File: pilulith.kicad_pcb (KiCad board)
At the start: 6 copper layers, 22 x 22 mm, 84 parts, among them J101 Conn_01x03_Pin, Q1 SBC847, SW101 CK_KMS2xxG, SW102 CK_KMS2xxG, U10 LIS2DH, U101 NRF52840-CKAA-F-R, U102 WLA.04, U103 ATECC608B-MAHDA, U104 LF21115TMR, U105 BME280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

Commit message: DRC passes
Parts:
- moved R112 0.51 mm to (157.5, 93.7)
- moved U10 0.08 mm to (159.4, 104.1)
- moved LS1 0.06 mm to (158.3, 111.1)
- moved C120 0.05 mm to (154.0, 96.5)
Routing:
- net GND: track 15.2 -> 16.8 mm, vias 94 -> 95
- net VCC: track 14.1 -> 15.4 mm, vias 29 -> 28
- net Net-(D112-K): track 0.84 -> 1.34 mm
- net /NFC2: vias 13 -> 5

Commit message: Removing additional warnings
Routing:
- net /IMU_INT: track 13.2 -> 11.3 mm, vias 3 -> 2
- net /DEC4_6: track 10.3 -> 8.72 mm, vias 11 -> 2
- net /LED02: vias 7 -> 3
- net /LED06: vias 5 -> 4
- net /LED07: vias 4 -> 3
- net /1.00/T0: vias 5 -> 4
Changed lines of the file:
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@@
 	)
 	(segment
+		(start 163.573771 100.892)
+		(end 163.573771 100.823833)
+		(width 0.0889)
+		(layer "F.Cu")
+		(net 3)
+	)
+	(segment
 		(start 161.919433 99.777445)
 		(end 162.527383 99.777445)
@@
 	)
 	(segment
-		(start 163.573771 100.823833)
-		(end 163.573771 100.892)
-		(width 0.0889)
-		(layer "F.Cu")
-		(net 3)
-	)
-	(segment
 		(start 161.574466 98.703224)
 		(end 161.574466 99.432478)
@@
 	)
 	(via
-		(at 163.577315 100.877)
-		(size 0.25)
-		(drill 0.15)
-		(layers "F.Cu" "B.Cu")
-		(net 3)
-	)
-	(via
-		(at 163.577315 100.877)
-		(size 0.25)
-		(drill 0.15)
-		(layers "F.Cu" "B.Cu")
-		(net 3)
-	)
-	(via
-		(at 163.577315 100.877)
-		(size 0.25)
-		(drill 0.15)
-		(layers "F.Cu" "B.Cu")
-		(net 3)
-	)
-	(via
-		(at 165.067051 100.587306)
-		(size 0.25)
-		(drill 0.15)
-		(layers "F.Cu" "B.Cu")
-		(net 3)
-	)
-	(via
-		(at 163.577315 100.877)
-		(size 0.25)
-		(drill 0.15)
-		(layers "F.Cu" "B.Cu")
-		(net 3)
-	)
-	(via
-		(at 163.577315 100.877)
-		(size 0.25)
-		(drill 0.15)
-		(layers "F.Cu" "B.Cu")
-		(net 3)
-	)
-	(via
-		(at 163.577315 100.877)
+		(at 163.573771 100.823833)
 		(size 0.25)
 		(drill 0.15)
@@
 		(net 3)
 	)
-	(via
-		(at 163.577315 100.877)
-		(size 0.25)
-		(drill 0.15)
-		(layers "F.Cu" "B.Cu")
-		(net 3)
-	)
-	(via
-		(at 163.577315 100.877)
-		(size 0.25)
-		(drill 0.15)
-		(layers "F.Cu" "B.Cu")
-		(net 3)
-	)
-	(via
-		(at 163.577315 100.877)
-		(size 0.25)
-		(drill 0.15)
-		(layers "F.Cu" "B.Cu")
-		(net 3)
-	)
 	(segment
 		(start 163.569013 98.052851)
@@
 	)
 	(segment
-		(start 164.777357 100.877)
-		(end 165.067051 100.587306)
-		(width 0.0889)
-		(layer "In3.Cu")
-		(net 3)
-	)
-	(segment
-		(start 163.577315 100.877)
-		(end 164.777357 100.877)
-		(width 0.0889)
-		(layer "In3.Cu")
-		(net 3)
-	)
-	(segment
 		(start 161.163245 95.539218)
 		(end 161.423463 95.279)
@@
 	)
 	(segment
-		(start 153.160814 96.228499)
-		(end 153.111314 96.278)
-		(width 0.0889)
-		(layer "In4.Cu")
-		(net 4)
-	)
-	(segment
-		(start 153.160814 96.228499)
+		(start 154.800314 94.588999)
 		(end 152.965315 96.423998)
 		(width 0.0889)
@@
 	)
 	(segment
-		(start 152.965315 96.423998)
-		(end 152.965315 96.66)
-		(width 0.0889)
-		(layer "In4.Cu")
-		(net 4)
-	)
-	(segment
 		(start 154.869314 94.52)
 		(end 154.800314 94.588999)
@@
 	)
 	(segment
-		(start 154.800314 94.588999)
-		(end 153.160814 96.228499)
+		(start 152.965315 96.423998)
+		(end 152.965315 96.66)
 		(width 0.0889)
 		(layer "In4.Cu")
@@
 	)
 	(segment
-		(start 159.492315 106.278)
-		(end 160.362315 106.278)
+		(start 159.501315 106.025)
+		(end 159.754315 106.278)
 		(width 0.0889)
 		(layer "F.Cu")
@@
 	(segment
 		(start 159.501315 105.424)
-		(end 159.492315 106.278)
+		(end 159.501315 106.025)
 		(width 0.0889)
 		(layer "F.Cu")
@@
 	)
 	(segment
-		(start 160.362315 106.278)
-		(end 160.574315 106.49)
+		(start 159.685313 104.762499)
+		(end 159.693315 105.265)
 		(width 0.0889)
 		(layer "F.Cu")
@@
 	)
 	(segment
-		(start 159.685313 104.762499)
-		(end 159.693315 105.265)
+		(start 159.754315 106.278)
+		(end 160.362315 106.278)
 		(width 0.0889)
 		(layer "F.Cu")
@@
 		(net 34)
 	)
-	(via
-		(at 160.066357 98.185648)
-		(size 0.25)
-		(drill 0.15)
-		(layers "F.Cu" "B.Cu")
-		(locked yes)
+	(segment
+		(start 160.362315 106.278)
+		(end 160.574315 106.49)
+		(width 0.0889)
+		(layer "F.Cu")
 		(net 34)
 	)
 	(via
-		(at 159.492315 106.278)
+		(at 160.066357 98.185648)
 		(size 0.25)
 		(drill 0.15)
 		(layers "F.Cu" "B.Cu")
+		(locked yes)
 		(net 34)
 	)
@@
 	)
 	(segment
-		(start 159.258463 98.287)
-		(end 159.058463 98.087)
-		(width 0.0889)
-		(layer "In3.Cu")
-		(net 34)
-	)
-	(segment
-		(start 159.058463 98.087)
-		(end 158.497463 98.087)
-		(width 0.0889)
-		(layer "In3.Cu")
-		(net 34)
-	)
-	(segment
-		(start 159.966898 98.287)
-		(end 159.258463 98.287)
-		(width 0.0889)
-		(layer "In3.Cu")
-		(net 34)
-	)
-	(segment
-		(start 160.067573 98.186325)
-		(end 159.966898 98.287)
-		(width 0.0889)
-		(layer "In3.Cu")
-		(net 34)
-	)
-	(segment
 		(start 159.941557 98.310448)
 		(end 159.941557 100.961767)
@@
 	)
 	(via
-		(at 166.922315 99.636)
-		(size 0.25)
-		(drill 0.15)
-		(layers "F.Cu" "B.Cu")
-		(net 50)
-	)
-	(via
-		(at 166.922315 99.636)
-		(size 0.25)
-		(drill 0.15)
-		(layers "F.Cu" "B.Cu")
-		(net 50)
-	)
-	(via
-		(at 166.922315 99.636)
-		(size 0.25)
-		(drill 0.15)
-		(layers "F.Cu" "B.Cu")
-		(net 50)
-	)
-	(via
-		(at 166.922315 99.636)
-		(size 0.25)
-		(drill 0.15)
-		(layers "F.Cu" "B.Cu")
-		(net 50)
-	)
-	(via
 		(at 168.729315 99.045)
 		(size 0.25)
@@
 	)
 	(via
-		(at 166.922315 99.636)
+		(at 166.928315 99.638)
 		(size 0.25)
 		(drill 0.15)
@@
 	)
 	(segment
+		(start 166.926315 99.636)
+		(end 166.928315 99.638)
+		(width 0.0889)
+		(layer "In3.Cu")
+		(net 50)
+	)
+	(segment
 		(start 164.987031 100.19545)
 		(end 164.746173 100.436308)
@@
 	)
 	(segment
+		(start 166.922315 99.636)
+		(end 166.926315 99.636)
+		(width 0.0889)
+		(layer "In3.Cu")
+		(net 50)
+	)
+	(segment
 		(start 155.354086 94.478)
 		(end 156.566544 94.478)
@@
 	)
 	(via
-		(at 159.185315 111.948)
+		(at 159.191315 111.946)
 		(size 0.25)
 		(drill 0.15)
@@
 	)
 	(via
-		(at 159.185315 111.948)
-		(size 0.25)
-		(drill 0.15)
-		(layers "F.Cu" "B.Cu")
-		(net 57)
-	)
-	(via
 		(at 162.436463 97.989)
 		(size 0.25)
@@
 	)
 	(segment
+		(start 159.189315 111.948)
+		(end 159.191315 111.946)
+		(width 0.0889)
+		(layer "In3.Cu")
+		(net 57)
+	)
+	(segment
+		(start 159.185315 111.948)
+		(end 159.189315 111.948)
+		(width 0.0889)
+		(layer "In3.Cu")
+		(net 57)
+	)
+	(segment
 		(start 159.185315 111.948)
 		(end 162.724315 111.948)
@@
 	)
 	(segment
-		(start 153.399315 112.579)
-		(end 153.450059 112.579)
+		(start 161.139463 95.131453)
+		(end 161.139463 94.068148)
 		(width 0.0889)
 		(layer "F.Cu")
@@
 	)
 	(segment
-		(start 161.139463 95.131453)
-		(end 161.139463 94.068148)
+		(start 160.860136 95.41078)
+		(end 161.139463 95.131453)
 		(width 0.0889)
 		(layer "F.Cu")
@@
 	)
 	(segment
-		(start 160.860136 95.41078)
-		(end 161.139463 95.131453)
+		(start 153.450059 112.579)
+		(end 153.398315 112.579)
 		(width 0.0889)
 		(layer "F.Cu")
@@
 	)
 	(segment
+		(start 153.398315 112.579)
+		(end 153.394315 112.583)
+		(width 0.0889)
+		(layer "F.Cu")
+		(net 58)
+	)
+	(segment
 		(start 153.450059 112.579)
 		(end 153.881059 113.01)
@@
 	)
 	(via
-		(at 160.757315 93.686)
-		(size 0.25)
-		(drill 0.15)
-		(layers "F.Cu" "B.Cu")
-		(net 58)
-	)
-	(via
-		(at 153.399315 112.579)
+		(at 153.394315 112.583)
 		(size 0.25)
 		(drill 0.15)
@@
 	)
 	(via
-		(at 153.399315 112.579)
+		(at 160.757315 93.686)
 		(size 0.25)
 		(drill 0.15)
@@
 		(size 0.25)
 		(drill 0.15)
-		(layers "F.Cu" "B.Cu")
-		(net 83)
-	)
-	(via
-		(at 161.959315 113.699)
-		(size 0.25)
-		(drill 0.15)

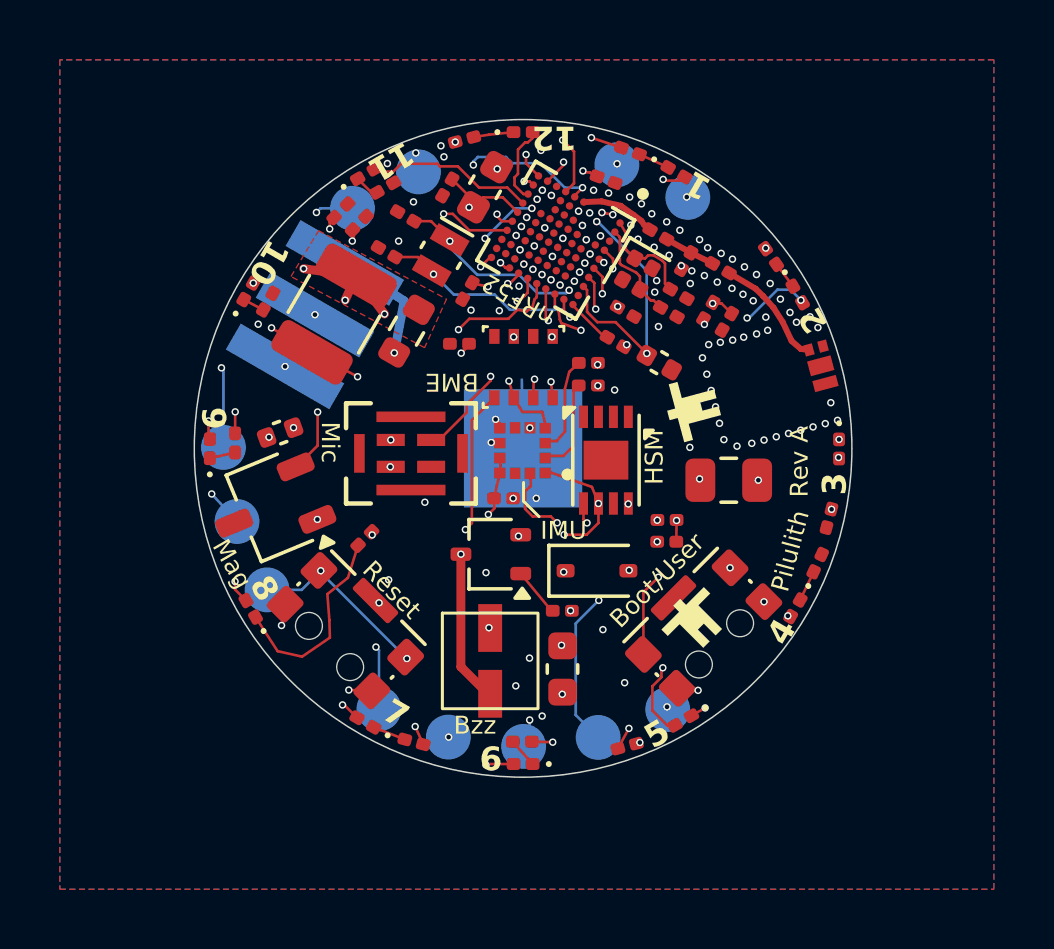
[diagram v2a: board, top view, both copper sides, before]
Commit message: added logo and changed for cheaper process. Found out it's a 22 mm board, whoops
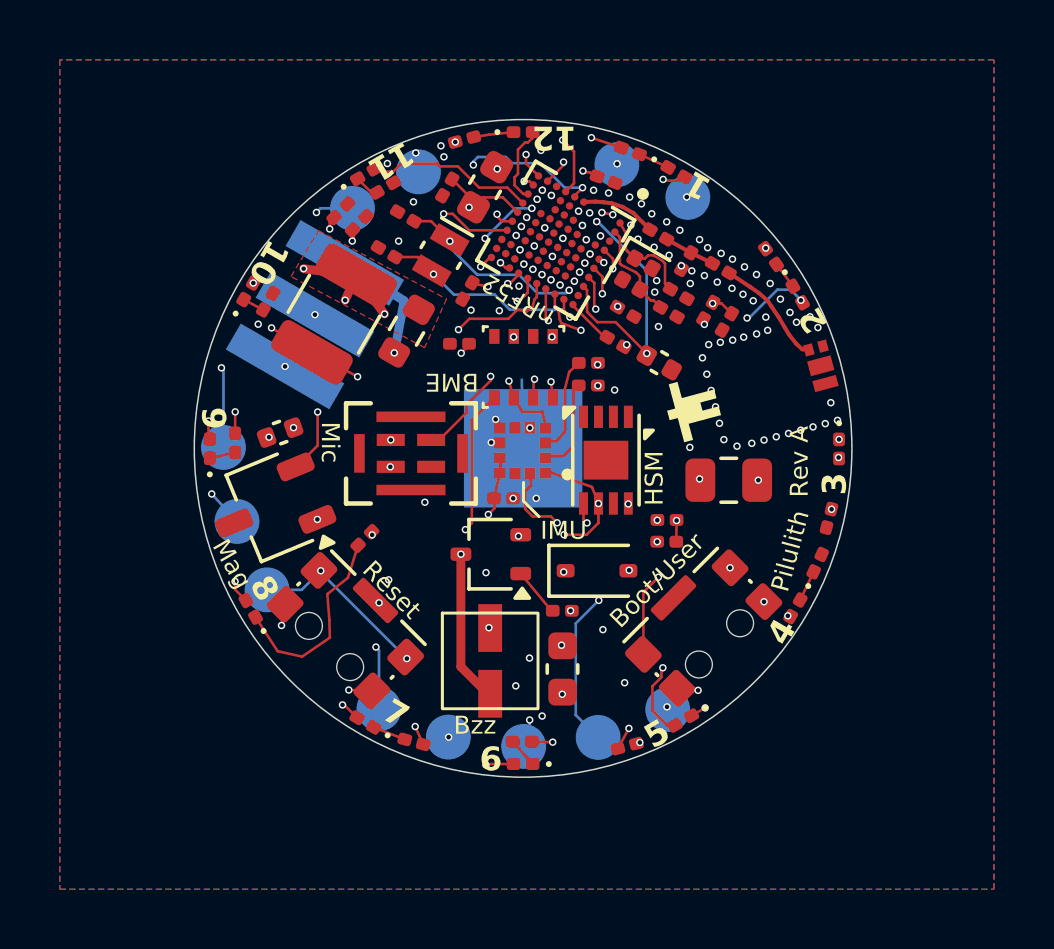
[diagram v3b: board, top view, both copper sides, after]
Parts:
- added G***: LOGO, pilulith:pilulith_10mm, B.Cu at (160.4, 109.2)
- G***: moved to B.Cu
- moved G*** 12.3 mm to (159.3, 99.0), turned to 0 degrees

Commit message: Rotated battery connector to match the spirulo board cabling
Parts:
- moved G*** 9.64 mm to (166.0, 101.4), turned to -135 degrees
- moved G*** 6.53 mm to (154.0, 102.9), turned to 60 degrees
- turned BT101 to 60 degrees
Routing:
- net /SDA: track 19.5 -> 20.7 mm
